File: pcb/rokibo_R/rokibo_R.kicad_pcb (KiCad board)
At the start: 2 copper layers, 125.1 x 85.3 mm, 46 parts, among them SW100 SW_Push, SW101 SW_Push, SW102 SW_Push, SW103 SW_Push, SW104 SW_Push, SW105 SW_Push, SW106 SW_Push, SW107 SW_Push, SW108 SW_Push, SW109 SW_Push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

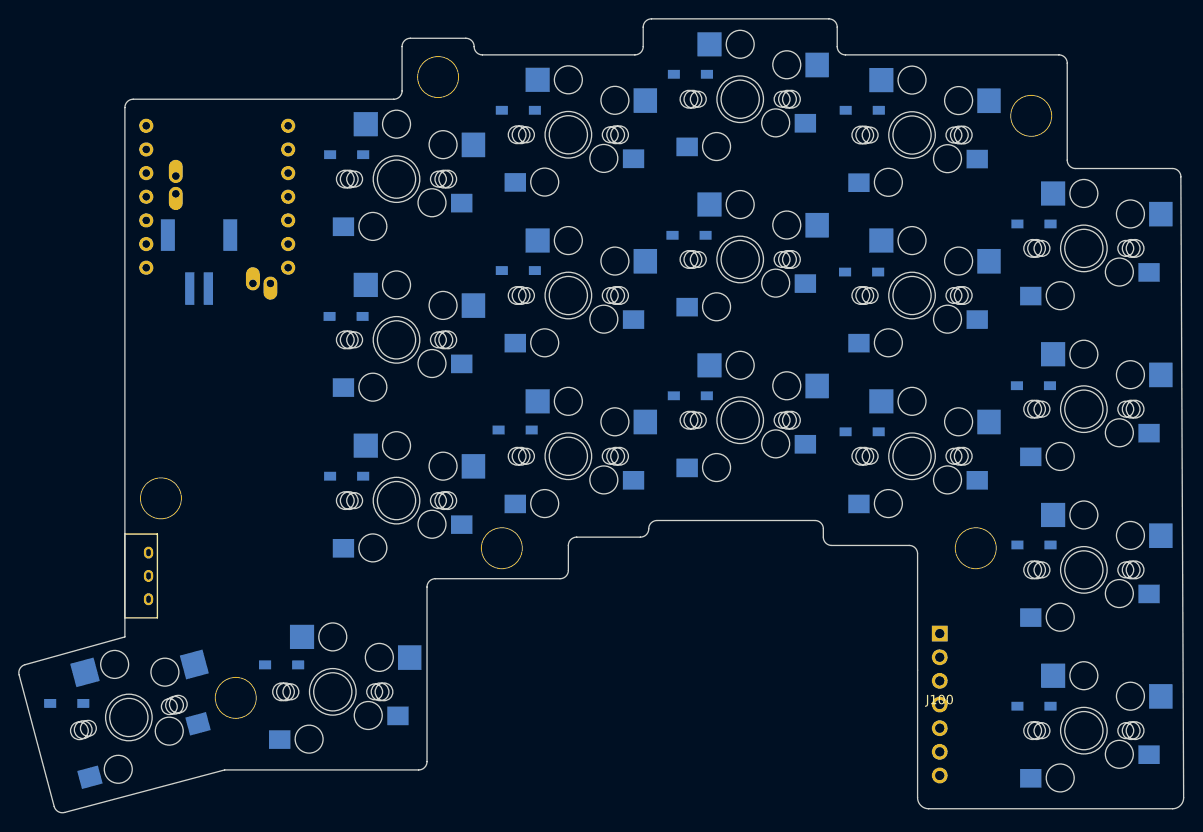
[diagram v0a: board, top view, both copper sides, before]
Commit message: fix: Use XIAO BLE footprint with hole
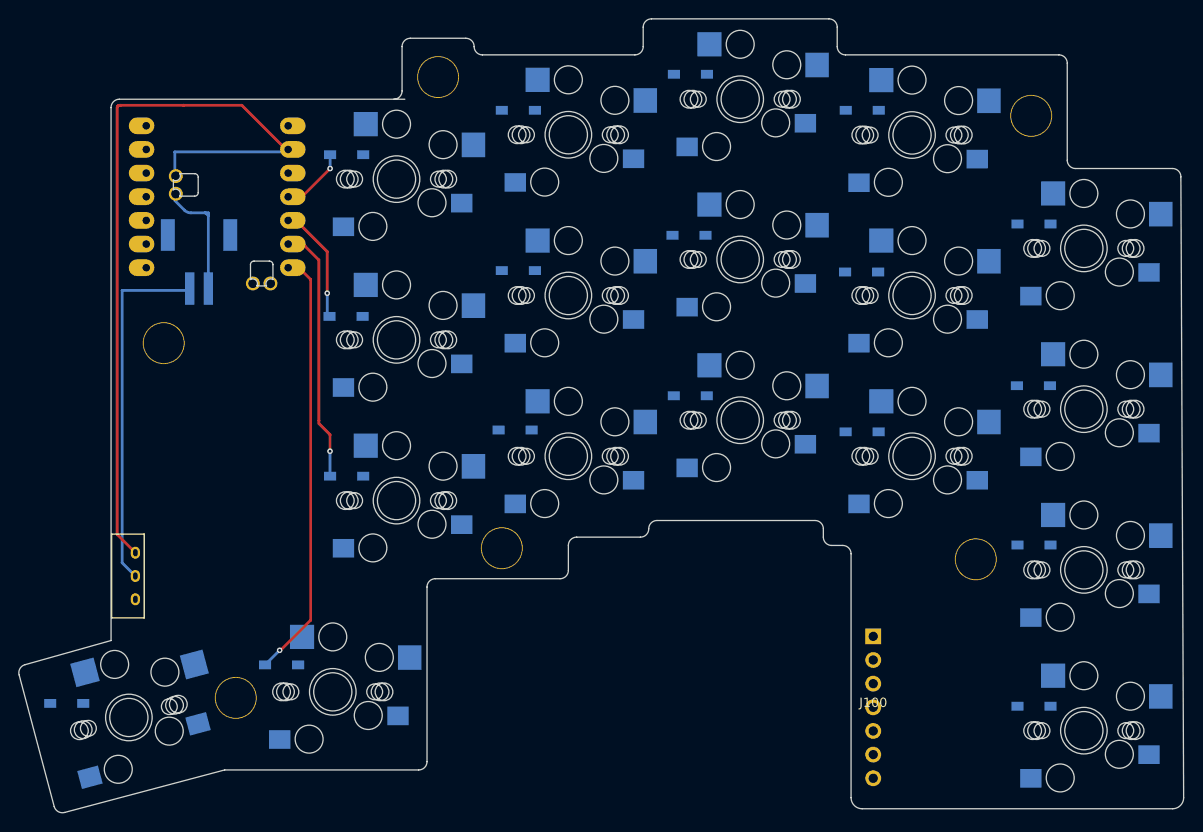
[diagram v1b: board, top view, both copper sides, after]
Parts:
- U100: footprint rokibo:XIAO_nRF52840_wBAT_wNFC -> rokibo:XIAO_nRF52840_wBAT_wNFC_1
- moved H104 16.7 mm to (86.9, 91.4)
- moved J100 7.15 mm to (163.1, 130.5)
- moved SW118 1.42 mm to (82.8, 116.4)
- moved H103 1.19 mm to (174.1, 114.6)
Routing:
- net GND: track 0.00 -> 83.6 mm
- net Row3: track 0.00 -> 46.4 mm, vias 0 -> 1
- net Net-(BT100--): track 0.00 -> 38.6 mm
- net Row2: track 0.00 -> 27.7 mm, vias 0 -> 1
- net VBat: track 0.00 -> 12.7 mm
- net Row1: track 0.00 -> 12.6 mm, vias 0 -> 1
- net Row0: track 0.00 -> 7.45 mm, vias 0 -> 1
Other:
- outline, holes or cut-outs redrawn

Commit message: fix: Update tracks
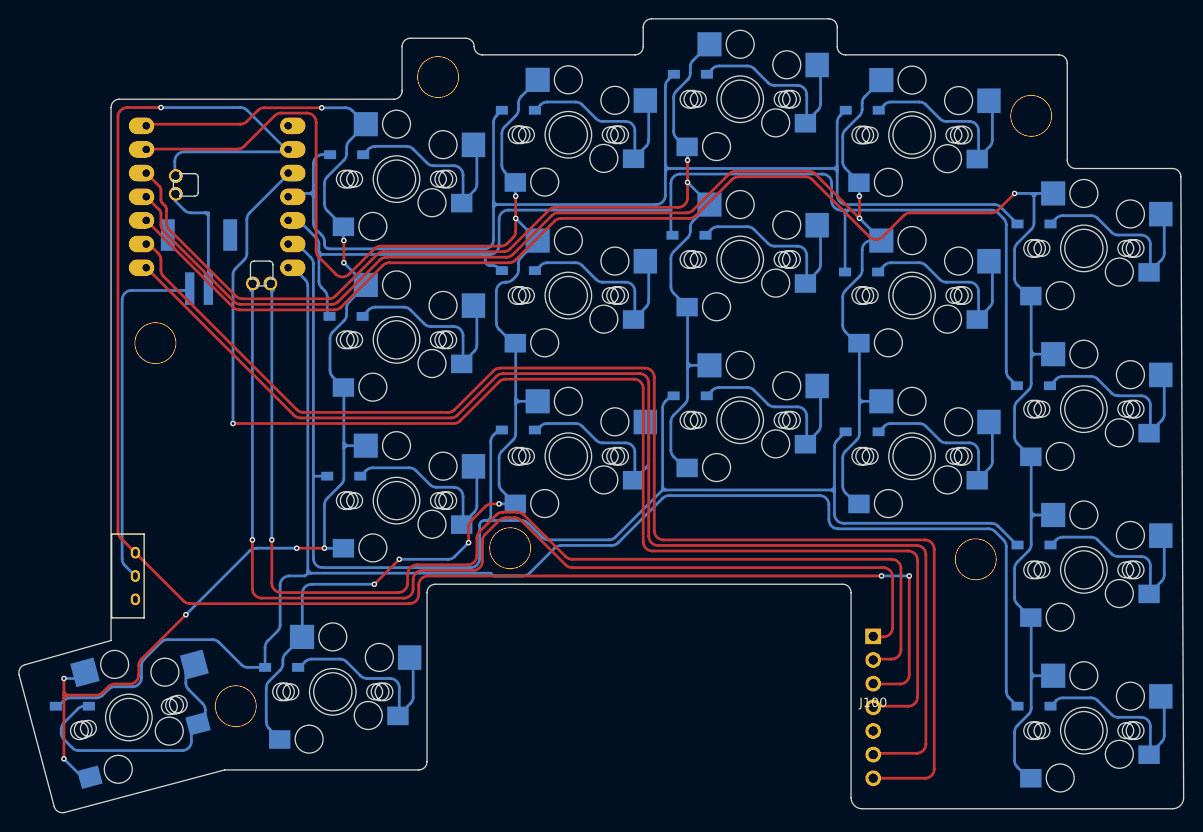
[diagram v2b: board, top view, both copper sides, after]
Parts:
- moved H104 0.89 mm to (86.0, 91.4)
- moved H102 0.89 mm to (124.1, 113.4)
- moved H105 0.89 mm to (94.7, 130.4)
- moved D103 0.68 mm to (77.1, 130.4)
- moved D106 0.35 mm to (125.0, 100.7)
- moved D102 0.31 mm to (106.3, 105.7)
- moved D107 0.27 mm to (99.6, 126.2)
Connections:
- U100 pad 15: MOTION -> SCLK
- U100 pad 16: SDIO -> CS
- U100 pad 6: SCLK -> MOTION
- U100 pad 7: CS -> SDIO
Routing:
- net Col4: track 0.00 -> 190.2 mm, vias 0 -> 1
- net Col1: track 0.00 -> 162.5 mm, vias 0 -> 6
- net Col3: track 0.00 -> 146.6 mm, vias 0 -> 2
- net MOTION: track 0.00 -> 143.7 mm
- net 3.3V: track 0.00 -> 142.7 mm, vias 0 -> 1
- net SDIO: track 0.00 -> 137.1 mm
- net Col0: track 0.00 -> 133.3 mm, vias 0 -> 8
- net Row3: track 46.4 -> 175.7 mm, vias 1 -> 0
- net Row2: track 27.7 -> 157.0 mm, vias 1 -> 0
- net Col2: track 0.00 -> 127.3 mm, vias 0 -> 2
- net Row0: track 7.45 -> 133.7 mm, vias 1 -> 0
- net CS: track 0.00 -> 120.5 mm, vias 0 -> 1
- net SCLK: track 0.00 -> 119.0 mm, vias 0 -> 1
- net Row1: track 12.6 -> 131.3 mm, vias 1 -> 0
- net GND: track 83.6 -> 184.8 mm, vias 0 -> 3
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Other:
- outline, holes or cut-outs redrawn
